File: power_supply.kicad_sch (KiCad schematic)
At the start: 28 parts, among them U1 AP63205WU, U2 LM66100DCK, U3 AP63203WU

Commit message: Reason about 3V3 LDO
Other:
- note added: "LDO after 3.3V buck converter not really worth it, as VCC and VCCA are directly connected inside WROOM 1 module. Eather continue using ESP32 ADC or connect high precition ADC via pin header to GPIOs or connect with bus"
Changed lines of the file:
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@@
 		(rev "1.0")
+	)
+	(text "LDO after 3.3V buck converter not really worth it, as\nVCC and VCCA are directly connected inside WROOM 1\nmodule. Eather continue using ESP32 ADC or connect high\nprecition ADC via pin header to GPIOs or connect with bus"
+		(exclude_from_sim no)
+		(at 199.898 106.934 0)
+		(effects
+			(font
+				(size 1.27 1.27)
+			)
+			(justify left)
+		)
 	)
 	(junction

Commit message: Undo component replacement
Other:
- note added: "LDO after 3.3V buck converter not worth it. VCC and VCCA are directly connected inside WROOM 1 module. Eather use ESP32 ADC and don't mind, or connect high precition ADC via pin header to GPIOs or connect with bus"
- note removed: "LDO after 3.3V buck converter not really worth it, as VCC and VCCA are directly connected inside WROOM 1 module. Eather continue using ESP32 ADC or connect high precition ADC via pin header to GPIOs or connect with bus"
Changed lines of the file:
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@@
 		(rev "1.0")
 	)
-	(text "LDO after 3.3V buck converter not really worth it, as\nVCC and VCCA are directly connected inside WROOM 1\nmodule. Eather continue using ESP32 ADC or connect high\nprecition ADC via pin header to GPIOs or connect with bus"
+	(text "LDO after 3.3V buck converter not worth it.\nVCC and VCCA are directly connected inside\nWROOM 1 module. Eather use ESP32 ADC and\ndon't mind, or connect high precition ADC via\npin header to GPIOs or connect with bus"
 		(exclude_from_sim no)
-		(at 199.898 106.934 0)
+		(at 202.184 107.442 0)
 		(effects
 			(font

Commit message: Add battery connector
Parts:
- added J8: Conn_01x02, Connector_JST:JST_XH_S2B-XH-A-1_1x02_P2.50mm_Horizontal, symbol Connector_Generic:Conn_01x02
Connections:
- net GND: now also J8.1 (Pin_1)
- net VBAT: now also J8.2 (Pin_2)
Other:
- moved on the sheet: C1, C10, C11, C12, C13, C14, C2, C3, C4, C5, C6, C7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

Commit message: Add missing pull-up for CP2102
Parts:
- renumbered J8 to J1

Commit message: Replace polyfuse with tube fuse
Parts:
- removed F1: Polyfuse, symbol Device:Polyfuse
- added F1: 6.3A, symbol Device:Fuse
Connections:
- net VBAT: now also F1.1
- net at TP4.1, U1.2 (EN), U1.3 (IN): now also F1.2
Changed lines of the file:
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@@
+	)
+	(symbol
+		(lib_id "Device:Fuse")
+		(at 96.52 68.58 90)
+		(unit 1)
+		(exclude_from_sim no)
+		(in_bom yes)
+		(on_board yes)
+		(dnp no)
+		(fields_autoplaced yes)
+		(property "Reference" "F1"
+			(at 96.52 62.23 90)
+			(effects
+				(font
+					(size 1.27 1.27)
+				)
+			)
+		)
+		(property "Value" "6.3A"
+			(at 96.52 64.77 90)
+			(effects
+				(font
+					(size 1.27 1.27)
+				)
+			)
+		)
+		(property "Footprint" ""
+			(at 96.52 70.358 90)
+			(effects
+				(font
+					(size 1.27 1.27)
+				)
+				(hide yes)
+			)
+		)
+		(property "Datasheet" "~"
+			(at 96.52 68.58 0)
+			(effects
+				(font
+					(size 1.27 1.27)
+				)
+				(hide yes)
+			)
+		)
+		(property "Description" "Fuse"
+			(at 96.52 68.58 0)
+			(effects
+				(font
+					(size 1.27 1.27)
+				)
+				(hide yes)
+			)
+		)
+		(property "LCSC Part" "C142706"
+			(at 96.52 68.58 90)
+			(effects
+				(font
+					(size 1.27 1.27)
+				)
+				(hide yes)
+			)
+		)
+		(pin "2"
+		)
+		(pin "1"
+		)
+		(instances
+			(project ""
+				(path "/f3fd8d79-9d35-4c04-811e-2697a2740958/003ca151-4f76-4d52-861b-70be86047379"
+					(reference "F1")
+					(unit 1)
+				)
+			)
+		)
 	)
 	(symbol
@@
 					(unit 1)
 				)
-			)
-		)
-	)
-	(symbol
-		(lib_id "Device:Polyfuse")
-		(at 96.52 68.58 90)
-		(unit 1)
-		(exclude_from_sim no)
-		(in_bom yes)
-		(on_board yes)
-		(dnp no)
-		(fields_autoplaced yes)
-		(property "Reference" "F1"
-			(at 96.52 62.23 90)
-			(effects
-				(font
-					(size 1.27 1.27)
-				)
-			)
-		)
-		(property "Value" "Polyfuse"
-			(at 96.52 64.77 90)
-			(effects
-				(font
-					(size 1.27 1.27)
-				)
-			)
-		)
-		(property "Footprint" ""
-			(at 101.6 67.31 0)
-			(effects
-				(font
-					(size 1.27 1.27)
-				)
-				(justify left)
-				(hide yes)
-			)
-		)
-		(property "Datasheet" "~"
-			(at 96.52 68.58 0)
-			(effects
-				(font
-					(size 1.27 1.27)
-				)
-				(hide yes)
-			)
-		)
-		(property "Description" "Resettable fuse, polymeric positive temperature coefficient"
-			(at 96.52 68.58 0)
-			(effects
-				(font
-					(size 1.27 1.27)
-				)
-				(hide yes)
-			)
-		)
-		(pin "1"
-		)
-		(pin "2"
-		)
-		(instances
-			(project "Tumbler2_Redesign"
-				(path "/f3fd8d79-9d35-4c04-811e-2697a2740958/003ca151-4f76-4d52-861b-70be86047379"
-					(reference "F1")
-					(unit 1)
-				)

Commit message: Assign fuse clips and add fuse to BOM
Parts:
- added F2: Fuse, symbol Device:Fuse
- F1: footprint (none) -> Fuse:Fuseholder_Clip-5x20mm_Littelfuse_100_Inline_P20.50x4.60mm_D1.30mm_Horizontal; LCSC Part C142706 -> C142797
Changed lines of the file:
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@@
 			)
 		)
-		(property "Footprint" ""
+		(property "Footprint" "Fuse:Fuseholder_Clip-5x20mm_Littelfuse_100_Inline_P20.50x4.60mm_D1.30mm_Horizontal"
 			(at 96.52 70.358 90)
 			(effects
@@
 			)
 		)
-		(property "Datasheet" "~"
+		(property "Datasheet" "https://www.lcsc.com/datasheet/C142797.pdf"
 			(at 96.52 68.58 0)
 			(effects
@@
 			)
 		)
-		(property "LCSC Part" "C142706"
+		(property "LCSC Part" "C142797"
 			(at 96.52 68.58 90)
 			(effects
@@
 					(unit 1)
 				)
+			)
+		)
+	)
+	(symbol
+		(lib_id "Device:Fuse")
+		(at 96.52 52.07 90)
+		(unit 1)
+		(exclude_from_sim no)
+		(in_bom yes)
+		(on_board no)
+		(dnp yes)
+		(fields_autoplaced yes)
+		(property "Reference" "F2"
+			(at 96.52 45.72 90)
+			(effects
+				(font
+					(size 1.27 1.27)
+				)
+			)
+		)
+		(property "Value" "Fuse"
+			(at 96.52 48.26 90)
+			(effects
+				(font
+					(size 1.27 1.27)
+				)
+			)
+		)
+		(property "Footprint" ""
+			(at 96.52 53.848 90)
+			(effects
+				(font
+					(size 1.27 1.27)
+				)
+				(hide yes)
+			)
+		)
+		(property "Datasheet" "~"
+			(at 96.52 52.07 0)
+			(effects
+				(font
+					(size 1.27 1.27)
+				)
+				(hide yes)
+			)
+		)
+		(property "Description" "Fuse"
+			(at 96.52 52.07 0)
+			(effects
+				(font
+					(size 1.27 1.27)
+				)
+				(hide yes)
+			)
+		)
+		(property "LCSC Part" "C142706"
+			(at 96.52 52.07 90)
+			(effects
+				(font
+					(size 1.27 1.27)
+				)
+				(hide yes)
+			)
+		)
+		(pin "2"
+		)
+		(pin "1"
+		)
+		(instances
+			(project ""
+				(path "/f3fd8d79-9d35-4c04-811e-2697a2740958/003ca151-4f76-4d52-861b-70be86047379"
+					(reference "F2")
+					(unit 1)
+				)

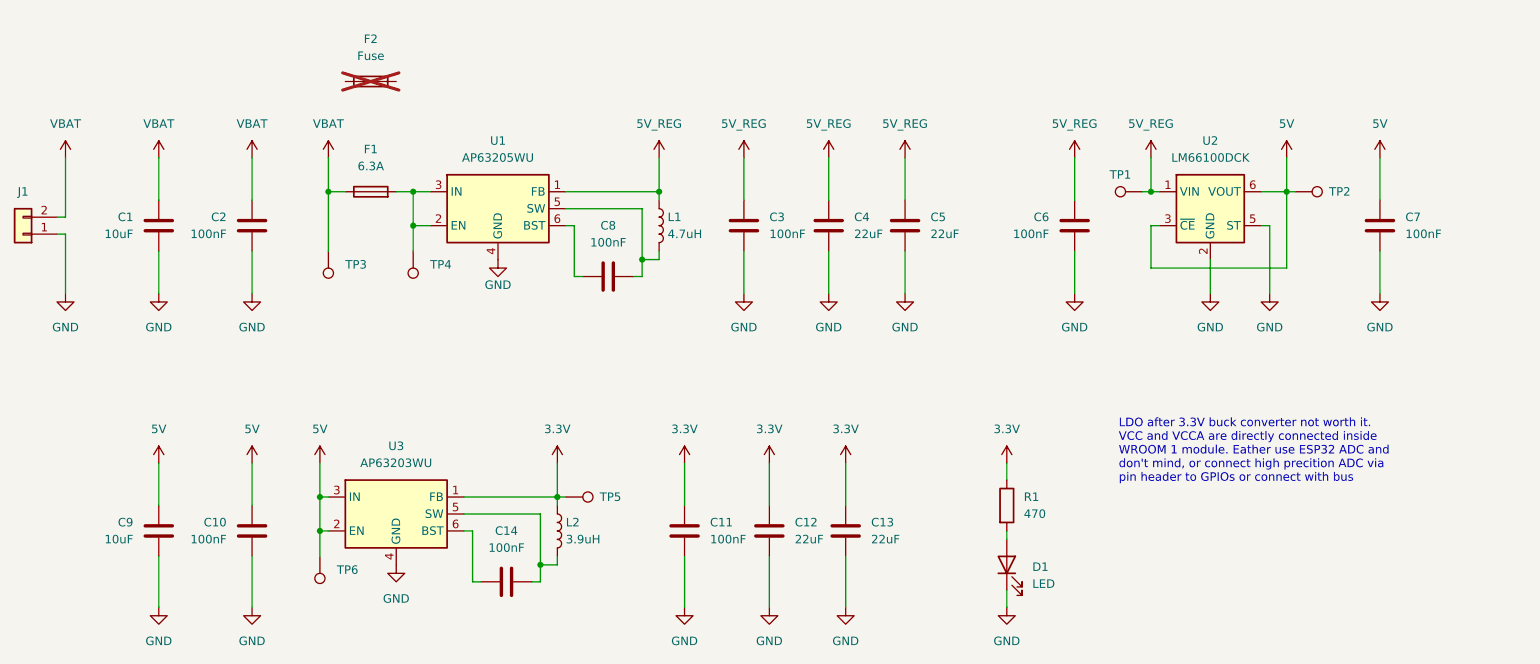
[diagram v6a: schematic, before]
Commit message: Move fuse to correct location
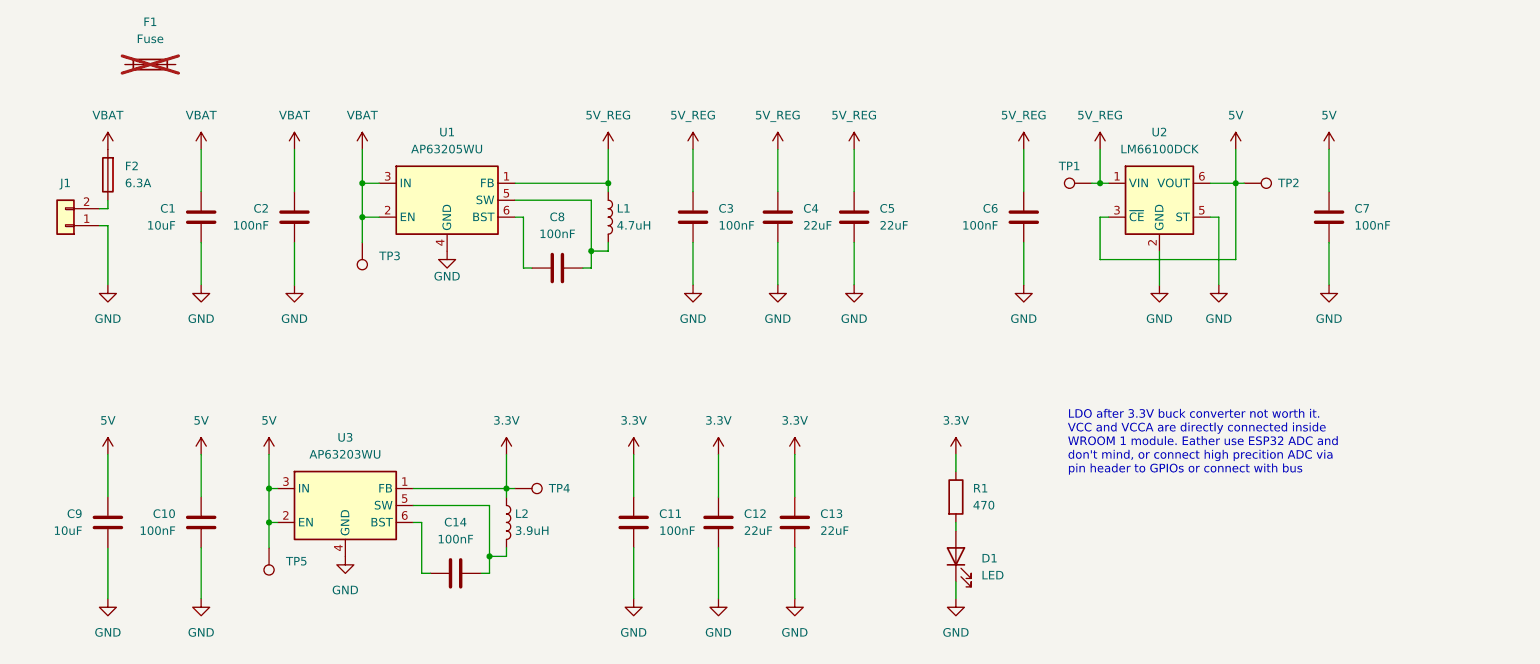
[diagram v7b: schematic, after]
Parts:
- removed TP3: TestPoint, symbol Connector:TestPoint
- renumbered F2 to F1, F1 to F2, TP4 to TP3, TP5 to TP4, TP6 to TP5
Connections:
- net VBAT: now also F2.2, TP3.1, U1.2 (EN), U1.3 (IN); no longer F2.1, J1.2 (Pin_2)
- new net: F2.1, J1.2 (Pin_2)
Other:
- moved on the sheet: C1, C10, C11, C12, C13, C14, C2, C3, C4, C5, C6, C7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

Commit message: Assign footprints and parts
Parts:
- removed F1: Fuse, symbol Device:Fuse
- C1, C9: LCSC Part (none) -> C96446
- C10, C11, C14, C2, C3, C6, C7, C8: footprint Capacitor_SMD:C_0402_1005Metric_Pad0.74x0.62mm_HandSolder -> Capacitor_SMD:C_0603_1608Metric_Pad1.08x0.95mm_HandSolder; LCSC Part (none) -> C14663
- C12, C13, C4, C5: LCSC Part (none) -> C2762594
- D1: LCSC Part (none) -> C965804
- F1: renamed from F2; value 6.3A -> 5A; footprint Fuse:Fuseholder_Clip-5x20mm_Littelfuse_100_Inline_P20.50x4.60mm_D1.30mm_Horizontal -> Fuse:Fuse_Littelfuse-NANO2-451_453; LCSC Part C142797 -> C66503
- J1: LCSC Part (none) -> C163035
- R1: value 470 -> 220; footprint (none) -> Resistor_SMD:R_0603_1608Metric_Pad0.98x0.95mm_HandSolder; LCSC Part (none) -> C107696
- TP1, TP2, TP3, TP4, TP5: footprint (none) -> TestPoint:TestPoint_Pad_D1.5mm
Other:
- note added: "Fuse is currently rated at 5 A. Short inrush currents exceed this value, but the fuse is slow-blow and therefore only trips after one minute at 200% of its rated current."
